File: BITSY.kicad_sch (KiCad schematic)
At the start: 6 parts, among them U1 MC68HC000FN, X1 16MHz

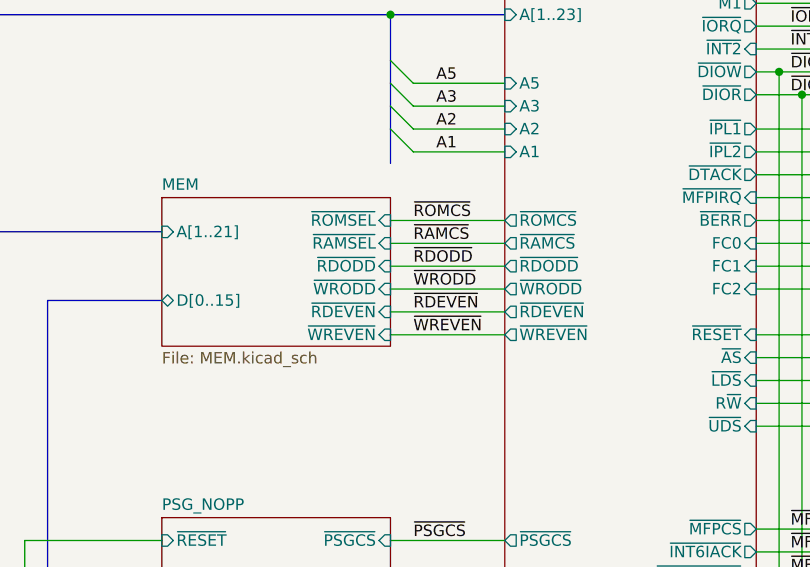
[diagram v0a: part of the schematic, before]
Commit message: V1C version of BITSY that uses an SRAM SIMM for memory.
This version sent to JLCPCB on 08/15/2025.
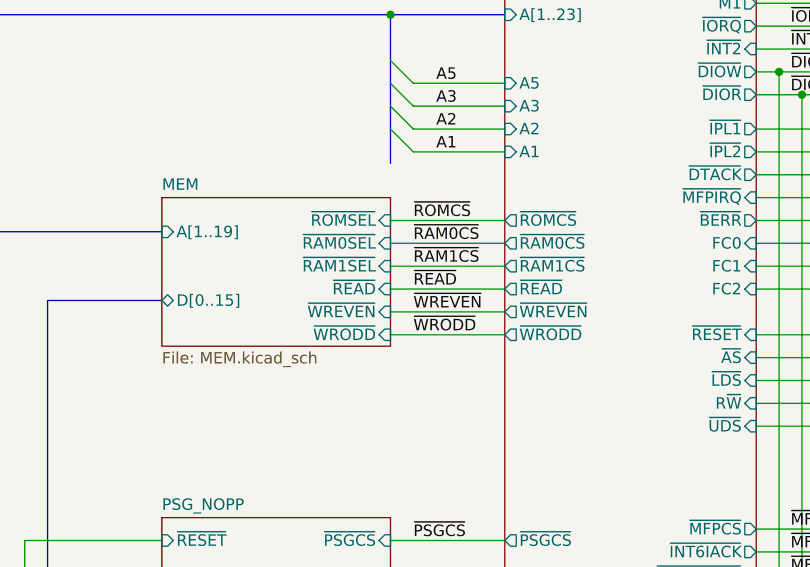
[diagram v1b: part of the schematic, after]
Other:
- sheet CONTROL ports: added ~{RAM0CS}, ~{RAM1CS}, ~{READ}; removed ~{RAMCS}, ~{RDEVEN}, ~{RDODD}
- sheet MEM ports: added A[1..19], ~{RAM0SEL}, ~{RAM1SEL}, ~{READ}; removed A[1..21], ~{RAMSEL}, ~{RDEVEN}, ~{RDODD}
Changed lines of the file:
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@@
 	(title_block
 		(title "BITSY Mark I - An MC68000 Single Board Computer")
-		(date "2025-06-12")
-		(rev "V1B")
-		(comment 1 "Licensed under CC-BY-SA-NC 4.0.")
+		(date "2025-08-15")
+		(rev "V1C")
+		(comment 1 "Licensed under CERN-OHL-S.")
 		(comment 2 "https://github.com/codesmythe/BITSY_MK_I")
 		(comment 3 "© 2025 Rob Gowin")
@@
 		)
 	)
-	(label "~{RDEVEN}"
-		(at 74.93 88.9 0)
+	(label "~{WRODD}"
+		(at 74.93 91.44 0)
 		(effects
 			(font
@@
 		)
 	)
-	(label "~{RDODD}"
+	(label "~{RAM1CS}"
 		(at 74.93 83.82 0)
 		(effects
@@
 		)
 	)
-	(label "~{RAMCS}"
+	(label "~{RAM0CS}"
 		(at 74.93 81.28 0)
 		(effects
@@
 	)
 	(label "~{WREVEN}"
-		(at 74.93 91.44 0)
+		(at 74.93 88.9 0)
 		(effects
 			(font
@@
 		)
 	)
-	(label "~{WRODD}"
+	(label "~{READ}"
 		(at 74.93 86.36 0)
 		(effects
@@
 			)
 		)
-		(pin "~{RAMSEL}" input
-			(at 72.39 81.28 0)
+		(pin "~{WRODD}" input
+			(at 72.39 91.44 0)
 			(effects
 				(font
@@
 			)
 		)
-		(pin "~{RDODD}" input
-			(at 72.39 83.82 0)
+		(pin "D[0..15]" tri_state
+			(at 46.99 87.63 180)
 			(effects
 				(font
 					(size 1.27 1.27)
 				)
-				(justify right)
+				(justify left)
 			)
 		)
-		(pin "~{WRODD}" input
-			(at 72.39 86.36 0)
+		(pin "~{WREVEN}" input
+			(at 72.39 88.9 0)
 			(effects
 				(font
@@
 			)
 		)
-		(pin "D[0..15]" tri_state
-			(at 46.99 87.63 180)
+		(pin "~{ROMSEL}" input
+			(at 72.39 78.74 0)
 			(effects
 				(font
 					(size 1.27 1.27)
 				)
-				(justify left)
+				(justify right)
 			)
 		)
-		(pin "~{RDEVEN}" input
-			(at 72.39 88.9 0)
+		(pin "~{RAM0SEL}" input
+			(at 72.39 81.28 0)
 			(effects
 				(font
@@
 			)
 		)
-		(pin "~{WREVEN}" input
-			(at 72.39 91.44 0)
+		(pin "~{RAM1SEL}" input
+			(at 72.39 83.82 0)
 			(effects
 				(font
@@
 			)
 		)
-		(pin "~{ROMSEL}" input
-			(at 72.39 78.74 0)
+		(pin "~{READ}" input
+			(at 72.39 86.36 0)
 			(effects
 				(font
@@
 			)
 		)
-		(pin "A[1..21]" input
+		(pin "A[1..19]" input
 			(at 46.99 80.01 180)
 			(effects
@@
 			)
 		)
-		(pin "~{RAMCS}" output
-			(at 85.09 81.28 180)
-			(effects
-				(font
-					(size 1.27 1.27)
-				)
-				(justify left)
-			)
-		)
 		(pin "~{RESET}" input
 			(at 113.03 91.44 0)
@@
 			)
 		)
-		(pin "~{RDODD}" output
-			(at 85.09 83.82 180)
-			(effects
-				(font
-					(size 1.27 1.27)
-				)
-				(justify left)
-			)
-		)
 		(pin "~{WRODD}" output
-			(at 85.09 86.36 180)
+			(at 85.09 91.44 180)
 			(effects
 				(font
@@
 		)
 		(pin "~{WREVEN}" output
-			(at 85.09 91.44 180)
-			(effects
-				(font
-					(size 1.27 1.27)
-				)
-				(justify left)
-			)
-		)
-		(pin "~{RDEVEN}" output
 			(at 85.09 88.9 180)
 			(effects
@@
 			(effects
 				(font
+					(size 1.27 1.27)
+				)
+				(justify left)
+			)
+		)
+		(pin "~{RAM0CS}" output
+			(at 85.09 81.28 180)
+			(effects
+				(font
+					(size 1.27 1.27)
+				)
+				(justify left)
+			)
+		)
+		(pin "~{RAM1CS}" output
+			(at 85.09 83.82 180)
+			(effects
+				(font
+					(size 1.27 1.27)
+				)
+				(justify left)
+			)
+		)
+		(pin "~{READ}" output
+			(at 85.09 86.36 180)
+			(effects
+				(font

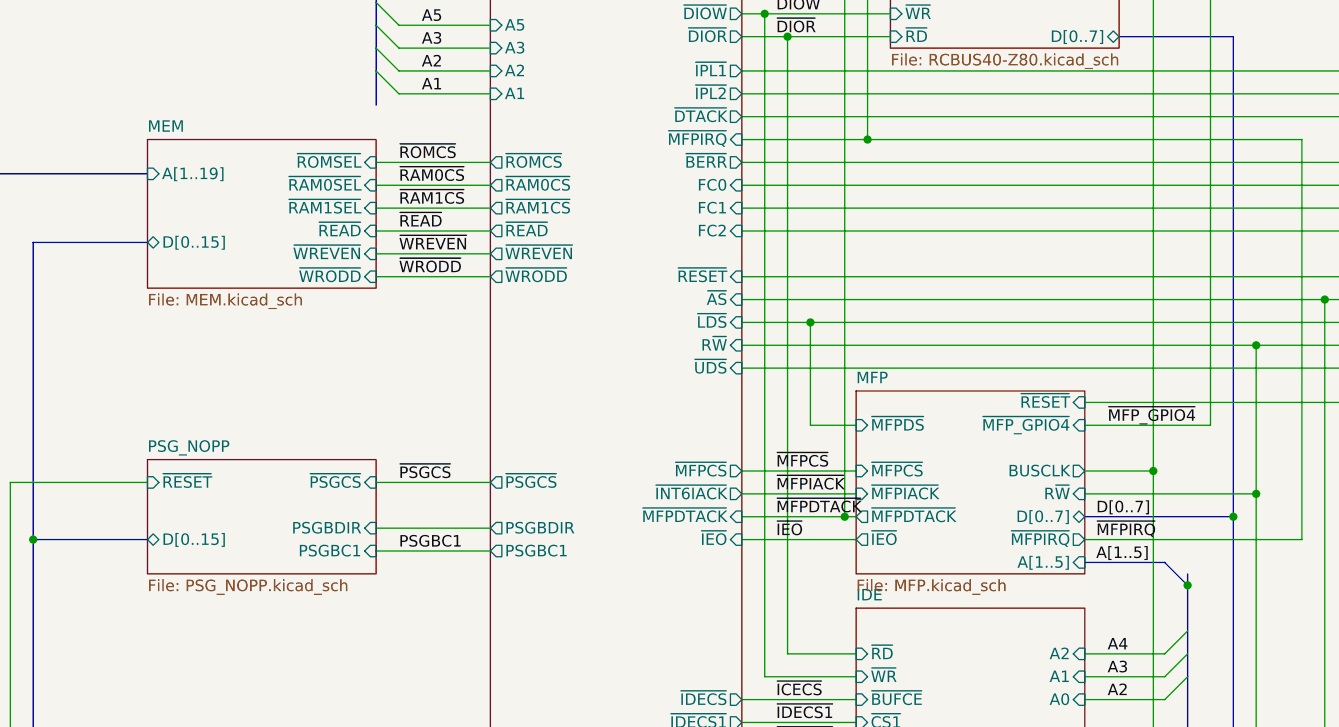
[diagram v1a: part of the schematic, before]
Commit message: Add two extra SIMM address lines.
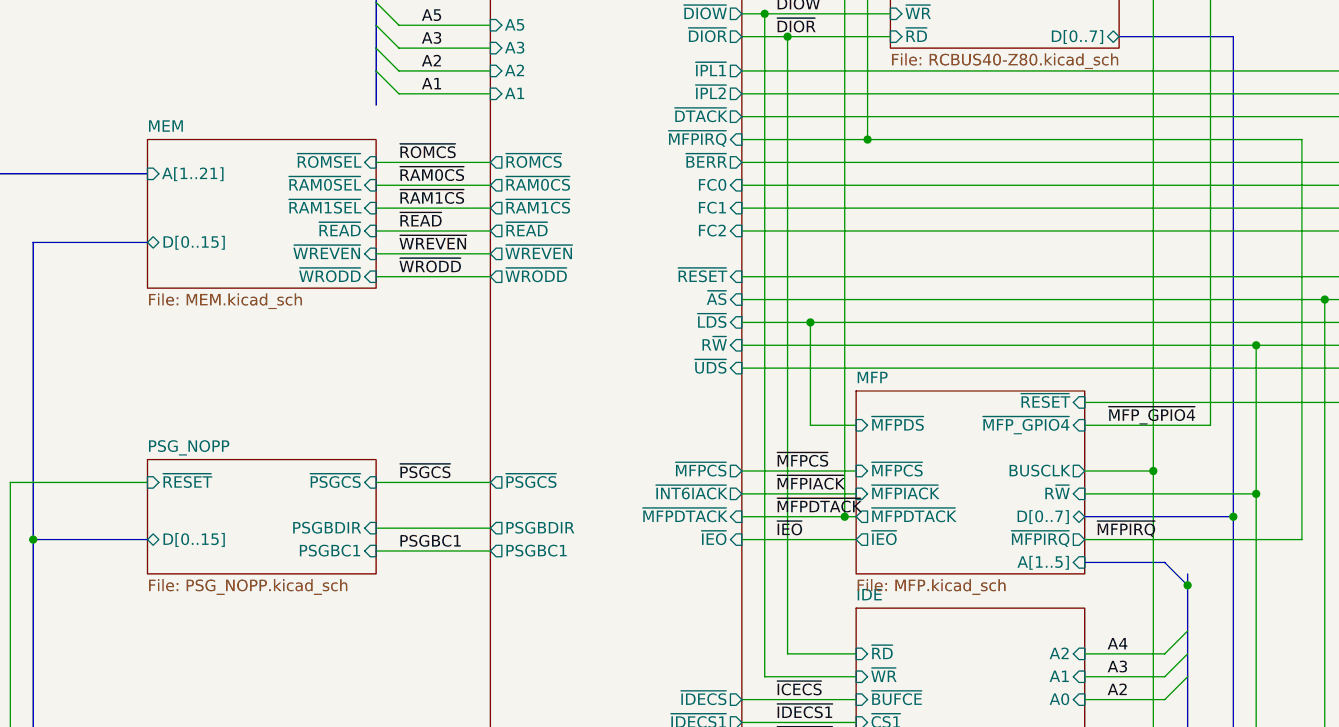
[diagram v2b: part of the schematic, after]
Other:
- sheet MEM ports: added A[1..21]; removed A[1..19]
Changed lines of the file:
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@@
-		)
-	)
-	(label "D[0..7]"
-		(at 152.4 118.11 0)
-		(effects
-			(font
-				(size 1.27 1.27)
-			)
-			(justify left bottom)
 		)
 	)
@@
 	(label "~{HALT}"
 		(at 194.31 44.45 0)
-		(effects
-			(font
-				(size 1.27 1.27)
-			)
-			(justify left bottom)
-		)
-	)
-	(label "A[1..5]"
-		(at 152.4 123.19 0)
 		(effects
 			(font
@@
 			)
 		)
-		(pin "A[1..19]" input
+		(pin "A[1..21]" input
 			(at 46.99 80.01 180)
 			(effects

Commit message: Update part numbers.
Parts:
- X1: PartNum00 815-ACH-16-EK -> 774-MXO45HST-3C-16.0
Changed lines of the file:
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@@
 			)
 		)
-		(property "PartNum00" "815-ACH-16-EK"
+		(property "PartNum00" "774-MXO45HST-3C-16.0"
 			(at 49.53 34.29 0)
 			(effects

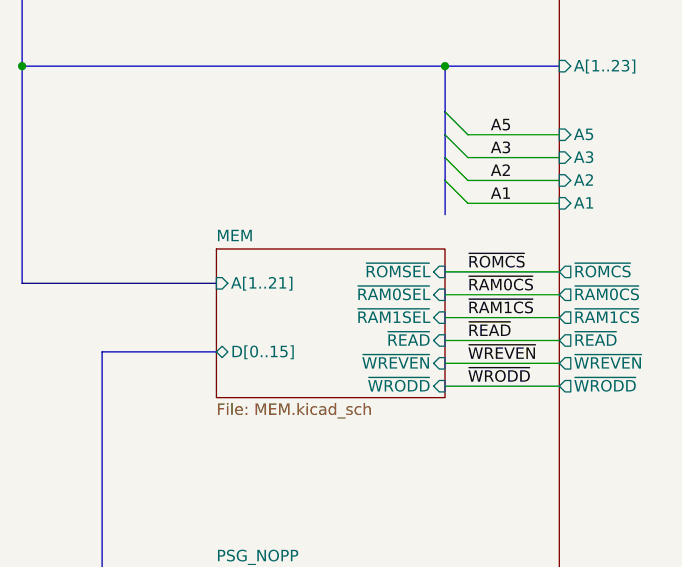
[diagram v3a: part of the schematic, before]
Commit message: Create V1E version.
Adds extra address line to SIMM for 16 MB support.
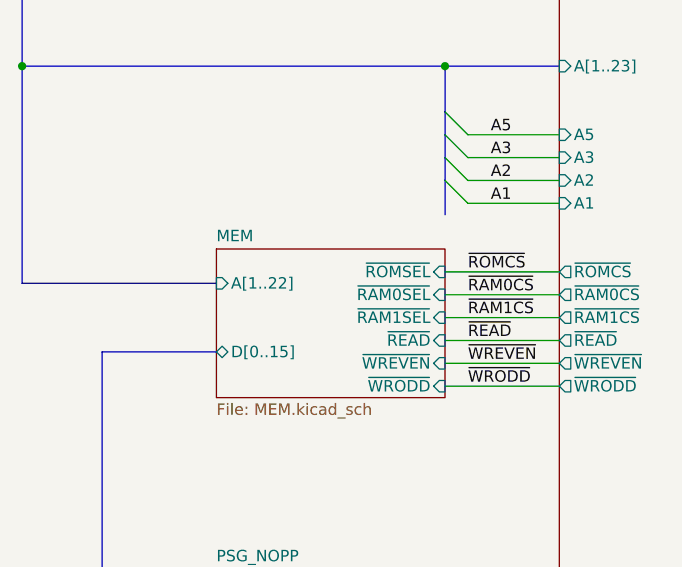
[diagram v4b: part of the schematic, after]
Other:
- sheet MEM ports: added A[1..22]; removed A[1..21]
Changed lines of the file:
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@@
 	(title_block
 		(title "BITSY Mark I - An MC68000 Single Board Computer")
-		(date "2025-08-15")
-		(rev "V1C")
+		(date "2025-11-09")
+		(rev "V1E")
 		(comment 1 "Licensed under CERN-OHL-S.")
 		(comment 2 "https://github.com/codesmythe/BITSY_MK_I")
@@
 			)
 		)
-		(pin "A[1..21]" input
+		(pin "A[1..22]" input
 			(at 46.99 80.01 180)
 			(effects
